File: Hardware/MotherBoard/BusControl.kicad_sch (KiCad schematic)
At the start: 3 parts, among them U6 4012, U7 4023, U8 4069

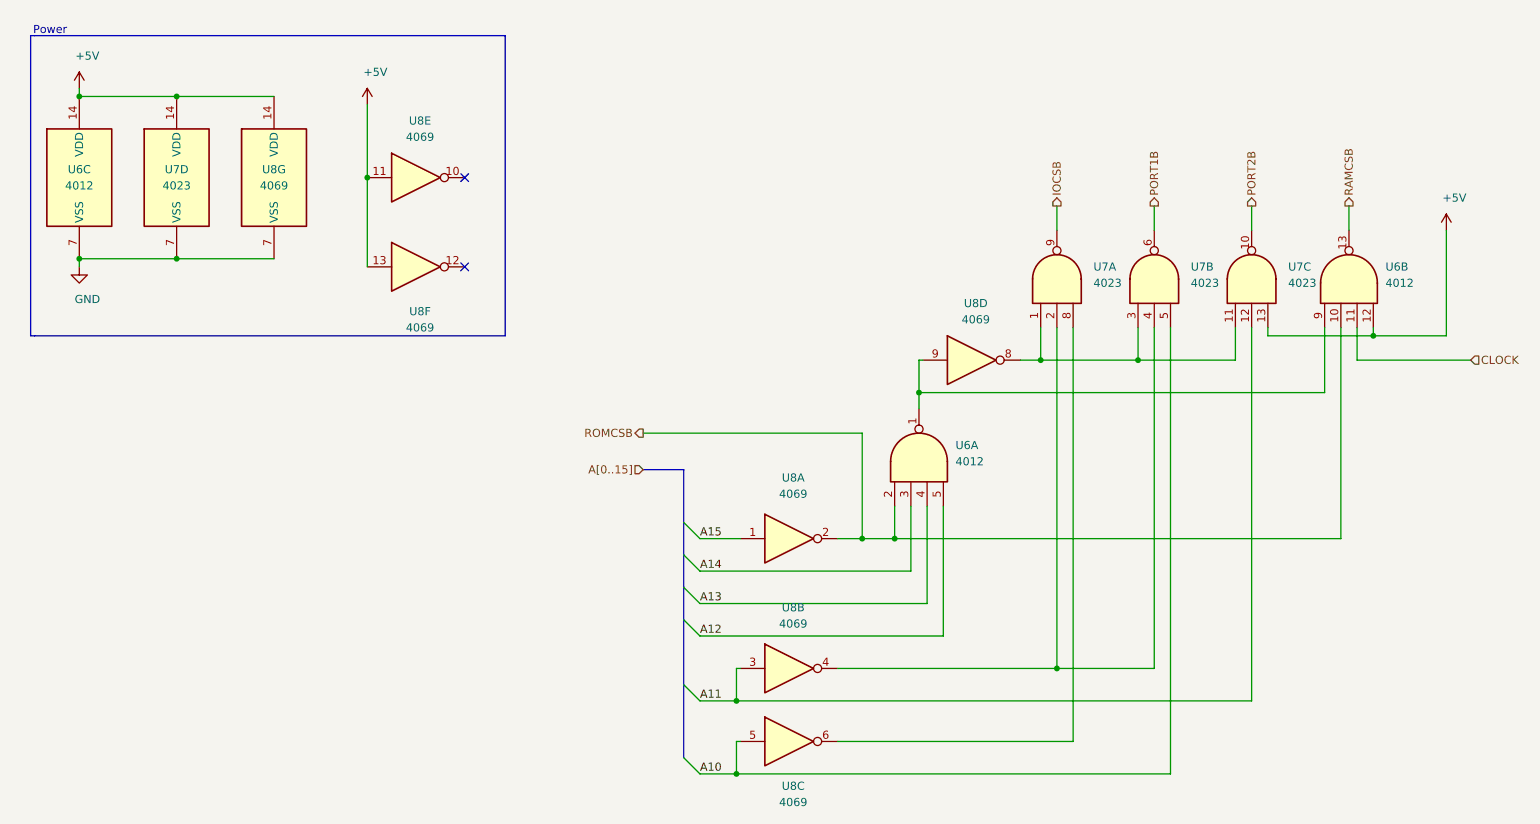
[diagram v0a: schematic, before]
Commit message: Add buffers to extenstion ports
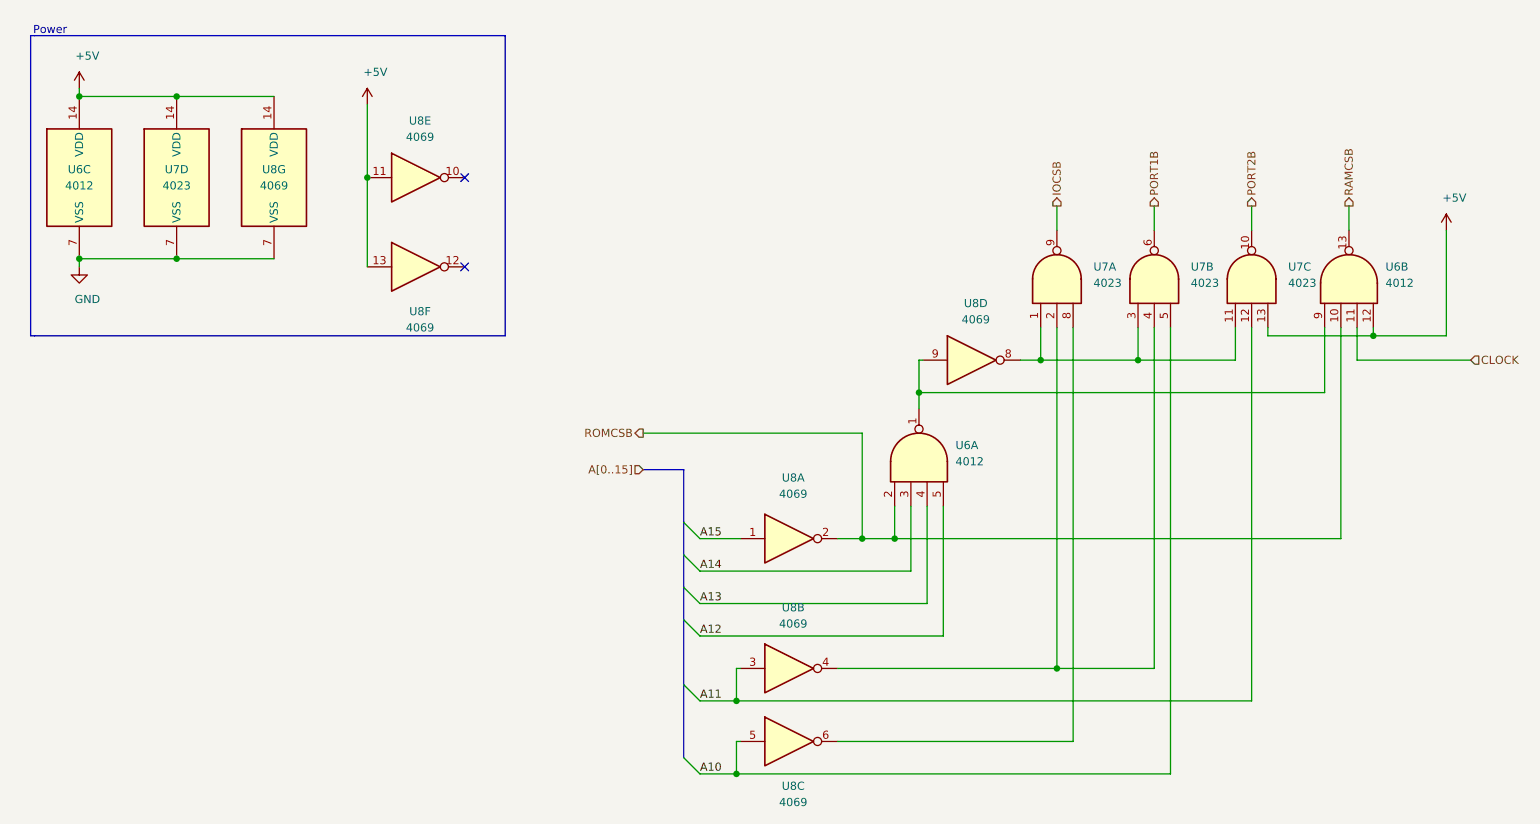
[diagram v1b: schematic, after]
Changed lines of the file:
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@@
-(kicad_sch (version 20200714) (host eeschema "(5.99.0-2358-g6d8fb94d8)")
-  (page 1 3)
+(kicad_sch (version 20201015) (generator eeschema)
+  (page 1 4)
   (paper "A4")
   (title_block
@@
   )
   (bus_alias "T" (members "RAMCSB" "IOCSB"))
-  (junction (at 30.48 31.75) (diameter 0) (color 0 0 0 0))
-  (junction (at 30.48 57.15) (diameter 0) (color 0 0 0 0))
-  (junction (at 45.72 31.75) (diameter 0) (color 0 0 0 0))
-  (junction (at 45.72 57.15) (diameter 0) (color 0 0 0 0))
-  (junction (at 75.565 44.45) (diameter 0) (color 0 0 0 0))
-  (junction (at 133.35 126.365) (diameter 0) (color 0 0 0 0))
-  (junction (at 133.35 137.795) (diameter 0) (color 0 0 0 0))
-  (junction (at 153.035 100.965) (diameter 0) (color 0 0 0 0))
-  (junction (at 158.115 100.965) (diameter 0) (color 0 0 0 0))
-  (junction (at 161.925 78.105) (diameter 0) (color 0 0 0 0))
-  (junction (at 180.975 73.025) (diameter 0) (color 0 0 0 0))
-  (junction (at 183.515 121.285) (diameter 0) (color 0 0 0 0))
-  (junction (at 196.215 73.025) (diameter 0) (color 0 0 0 0))
-  (junction (at 233.045 69.215) (diameter 0) (color 0 0 0 0))
+  (junction (at 30.48 31.75) (diameter 1.016) (color 0 0 0 0))
+  (junction (at 30.48 57.15) (diameter 1.016) (color 0 0 0 0))
+  (junction (at 45.72 31.75) (diameter 1.016) (color 0 0 0 0))
+  (junction (at 45.72 57.15) (diameter 1.016) (color 0 0 0 0))
+  (junction (at 75.565 44.45) (diameter 1.016) (color 0 0 0 0))
+  (junction (at 133.35 126.365) (diameter 1.016) (color 0 0 0 0))
+  (junction (at 133.35 137.795) (diameter 1.016) (color 0 0 0 0))
+  (junction (at 153.035 100.965) (diameter 1.016) (color 0 0 0 0))
+  (junction (at 158.115 100.965) (diameter 1.016) (color 0 0 0 0))
+  (junction (at 161.925 78.105) (diameter 1.016) (color 0 0 0 0))
+  (junction (at 180.975 73.025) (diameter 1.016) (color 0 0 0 0))
+  (junction (at 183.515 121.285) (diameter 1.016) (color 0 0 0 0))
+  (junction (at 196.215 73.025) (diameter 1.016) (color 0 0 0 0))
+  (junction (at 233.045 69.215) (diameter 1.016) (color 0 0 0 0))
+  (no_connect (at 90.805 44.45))
   (no_connect (at 90.805 58.42))
-  (no_connect (at 90.805 44.45))
   (bus_entry (at 125.095 98.425) (size 2.54 2.54)
     (stroke (width 0.1524) (type solid) (color 0 0 0 0))
@@
     (stroke (width 0) (type solid) (color 0 0 0 0))
   )
-  (bus (pts (xy 125.095 90.17) (xy 125.095 103.505))
-    (stroke (width 0) (type solid) (color 0 0 0 0))
-  )
-  (bus (pts (xy 125.095 103.505) (xy 125.095 113.665))
-    (stroke (width 0) (type solid) (color 0 0 0 0))
-  )
-  (bus (pts (xy 125.095 113.665) (xy 125.095 135.255))
+  (bus (pts (xy 125.095 90.17) (xy 125.095 98.425))
+    (stroke (width 0) (type solid) (color 0 0 0 0))
+  )
+  (bus (pts (xy 125.095 98.425) (xy 125.095 103.505))
+    (stroke (width 0) (type solid) (color 0 0 0 0))
+  )
+  (bus (pts (xy 125.095 103.505) (xy 125.095 108.585))
+    (stroke (width 0) (type solid) (color 0 0 0 0))
+  )
+  (bus (pts (xy 125.095 108.585) (xy 125.095 113.665))
+    (stroke (width 0) (type solid) (color 0 0 0 0))
+  )
+  (bus (pts (xy 125.095 113.665) (xy 125.095 123.825))
+    (stroke (width 0) (type solid) (color 0 0 0 0))
+  )
+  (bus (pts (xy 125.095 123.825) (xy 125.095 135.255))
     (stroke (width 0) (type solid) (color 0 0 0 0))
   )
@@
   (symbol (lib_id "power:+5V") (at 30.48 30.48 0) (unit 1)
     (in_bom yes) (on_board yes)
-    (property "Reference" "#PWR026" (id 0) (at 30.48 34.29 0)
+    (property "Reference" "#PWR0123" (id 0) (at 30.48 34.29 0)
       (effects (font (size 1.27 1.27)) hide)
     )
@@
   (symbol (lib_id "power:+5V") (at 75.565 33.02 0) (unit 1)
     (in_bom yes) (on_board yes)
-    (property "Reference" "#PWR028" (id 0) (at 75.565 36.83 0)
+    (property "Reference" "#PWR0122" (id 0) (at 75.565 36.83 0)
       (effects (font (size 1.27 1.27)) hide)
     )
@@
   (symbol (lib_id "power:+5V") (at 244.475 52.705 0) (unit 1)
     (in_bom yes) (on_board yes)
-    (property "Reference" "#PWR029" (id 0) (at 244.475 56.515 0)
+    (property "Reference" "#PWR0124" (id 0) (at 244.475 56.515 0)
       (effects (font (size 1.27 1.27)) hide)
     )
@@
   (symbol (lib_id "power:GND") (at 30.48 58.42 0) (unit 1)
     (in_bom yes) (on_board yes)
-    (property "Reference" "#PWR027" (id 0) (at 30.48 64.77 0)
-      (effects (font (size 1.27 1.27)) hide)
-    )
+    (property "Reference" "#PWR0121" (id 0) (at 30.48 64.77 0)
+      (effects (font (size 1.27 1.27)) hide)
+    )

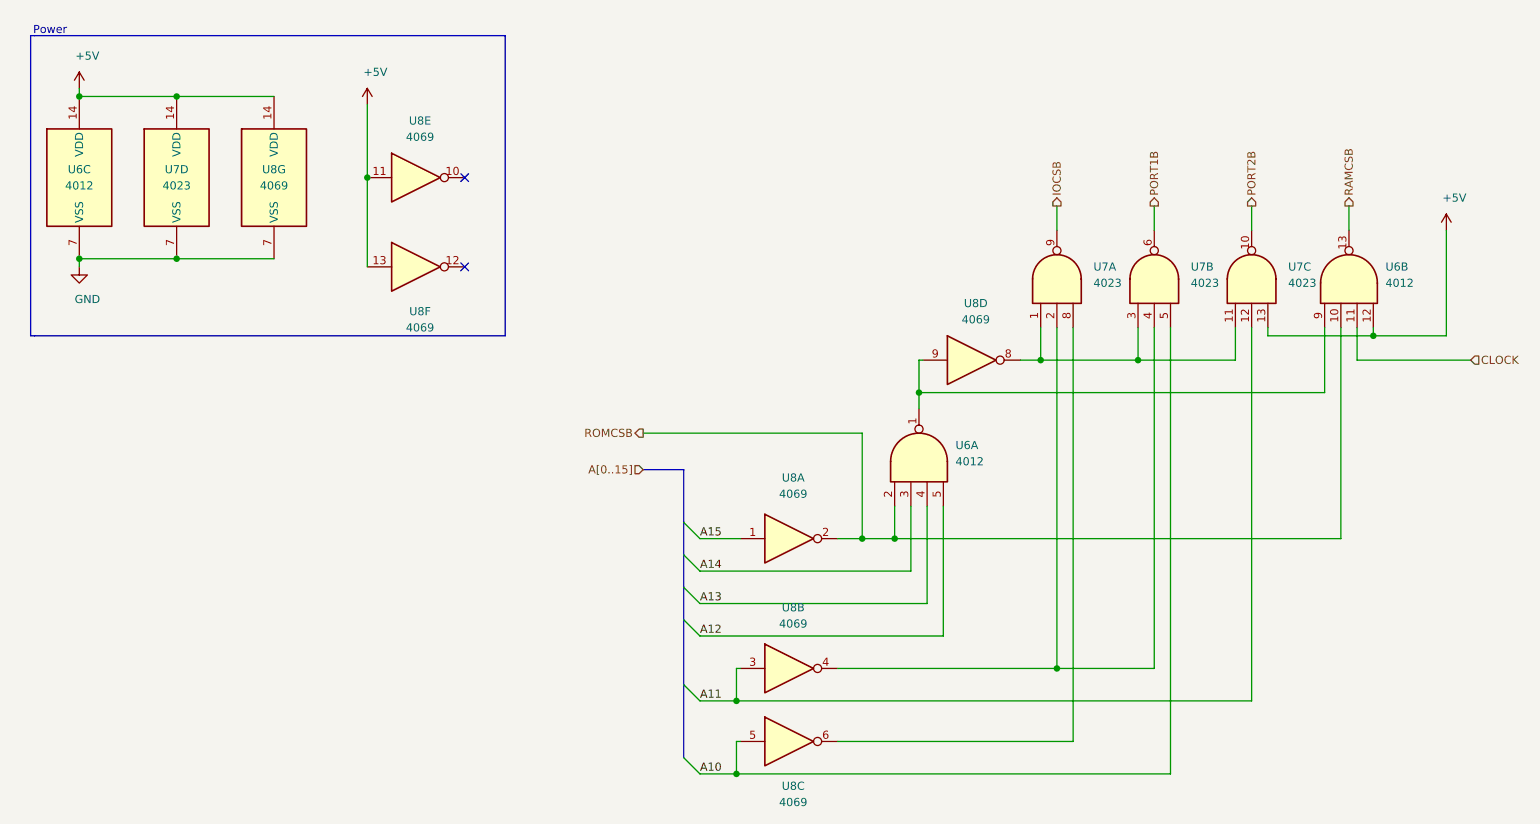
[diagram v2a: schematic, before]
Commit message: Replace logic IC 4xxx by 74hcxx
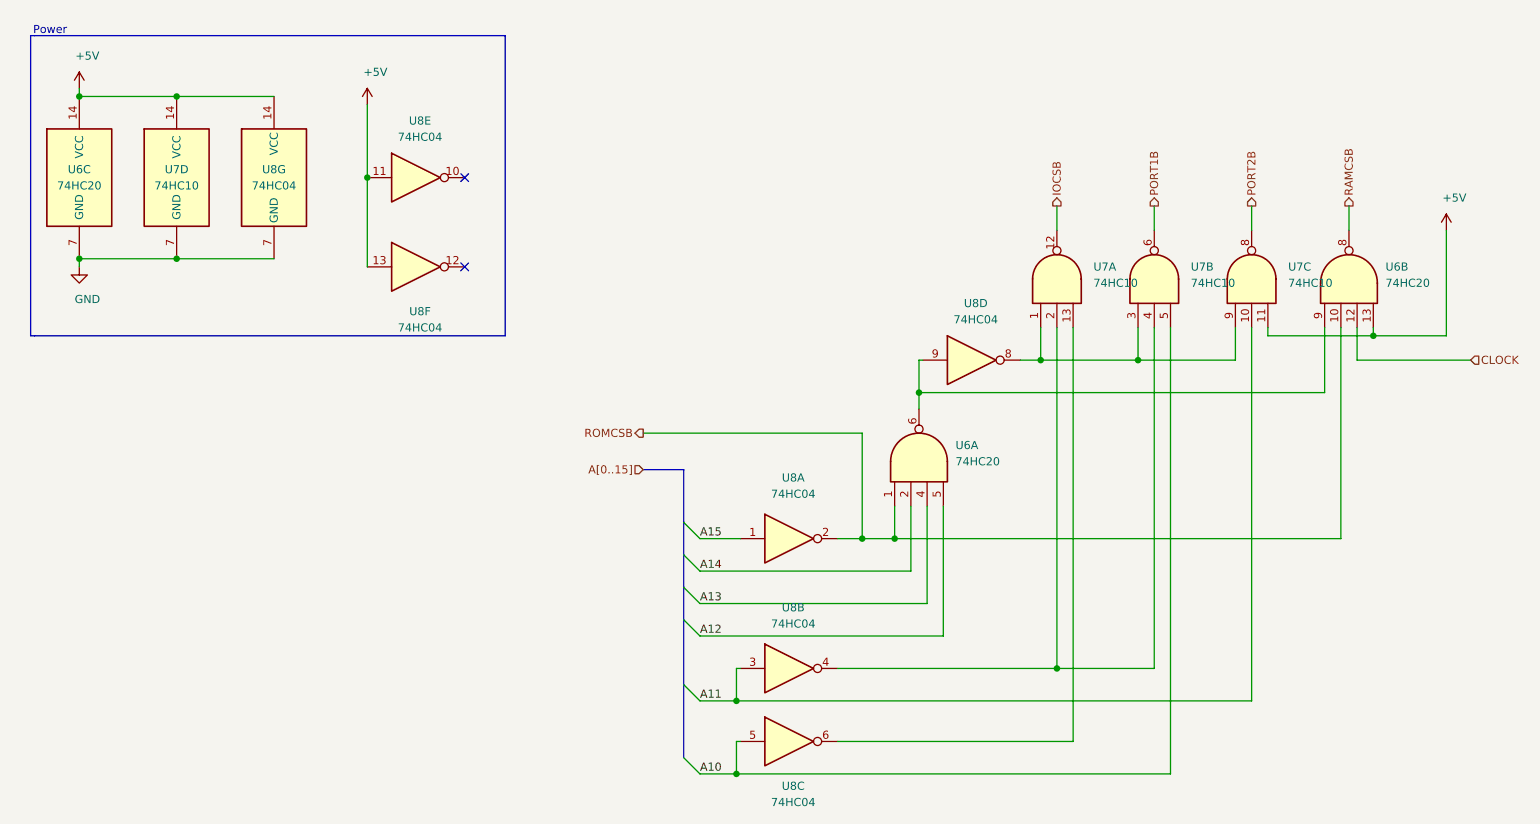
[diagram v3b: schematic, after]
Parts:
- U6: value 4012 -> 74HC20; symbol 4xxx:4012 -> 74xx:74LS20
- U7: value 4023 -> 74HC10; symbol 4xxx:4023 -> 74xx:74LS10
- U8: value 4069 -> 74HC04; symbol 4xxx:4069 -> 74xx:74LS04
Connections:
- net +5V: now also U6.13, U7.11; no longer U6.12, U7.13
- net A11: now also U7.10; no longer U7.12
- net A14: now also U6.2; no longer U6.3
- net CLOCK: now also U6.12; no longer U6.11
- net IOCSB: now also U7.12; no longer U7.9
- net PORT2B: now also U7.8; no longer U7.10
- net RAMCSB: now also U6.8; no longer U6.13
- net ROMCSB: now also U6.1; no longer U6.2
- net at U7.1, U7.3, U8.8: now also U7.9; no longer U7.11
- net at U8.6: now also U7.13; no longer U7.8
- net at U6.9, U8.9: now also U6.6; no longer U6.1

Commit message: Version 1.2
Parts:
- removed U6: 74HC20, Package_DIP:DIP-14_W7.62mm, symbol 74xx:74LS20
- removed U7: 74HC10, Package_DIP:DIP-14_W7.62mm, symbol 74xx:74LS10
- removed U8: 74HC04, Package_DIP:DIP-14_W7.62mm, symbol 74xx:74LS04
- added C9: 220nF, Capacitor_THT:C_Disc_D5.0mm_W2.5mm_P5.00mm, symbol Device:C_Small
- added U6: 74HC148, Package_DIP:DIP-16_W7.62mm, symbol 74xx:74LS148
- added U7: 74HC574, Package_DIP:DIP-20_W7.62mm, symbol 74xx:74HCT574
- added U8: ATF16V8B, Package_DIP:DIP-20_W7.62mm, symbol Logic_Programmable:GAL16V8
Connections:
- net +5V: now also C9.1, U6.1 (I4), U6.12 (I2), U6.13 (I3), U6.16 (VCC), U6.2 (I5), U6.3 (I6), U6.4 (I7), U7.20 (VCC), U8.20 (VCC)
- net A10: now also U8.7 (I7)
- net A11: now also U8.6 (I6)
- net A12: now also U8.5 (I5)
- net A13: now also U8.4 (I4)
- net A14: now also U8.3 (I3)
- net A15: now also U8.2 (I2)
- net CLOCK: now also U7.11 (Cp), U8.1 (I1/CLK)
- net GND: now also C9.2, U6.5 (EI), U6.8 (GND), U7.10 (GND), U7.2 (D0), U7.6 (D4), U7.7 (D5), U7.8 (D6), U7.9 (D7), U8.10 (GND)
- net IOCSB: now also U8.19 (IO1)
- net PORT1B: now also U8.18 (IO2)
- net PORT2B: now also U8.17 (I03)
- net RAMCSB: now also U8.15 (IO5)
- net ROMCSB: now also U8.14 (IO6)
- new net: U6.6 (S2), U7.5 (D3)
- new net: U6.7 (S1), U7.4 (D2)
- new net: U6.9 (S0), U7.3 (D1)
- new net: U7.1 (OE), U8.16 (IO4)
- new net A8: U8.9 (I9)
- new net A9: U8.8 (I8)
- new net D0: U7.19 (Q0)
- new net D1: U7.18 (Q1)
- new net D2: U7.17 (Q2)
- new net D3: U7.16 (Q3)
- new net D4: U7.15 (Q4)
- new net D5: U7.14 (Q5)
- new net D6: U7.13 (Q6)
- new net D7: U7.12 (Q7)
- new net IRQ0B: U6.10 (IO)
- new net IRQ1B: U6.11 (I1)
- new net IRQB: U6.14 (GS)
- new net RDYB: U8.11 (I10/~OE~)
- no-connect marks 2 -> 3
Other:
- note added: "Filters"
- note removed: "Power"
